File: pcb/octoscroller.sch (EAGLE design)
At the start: 5 parts

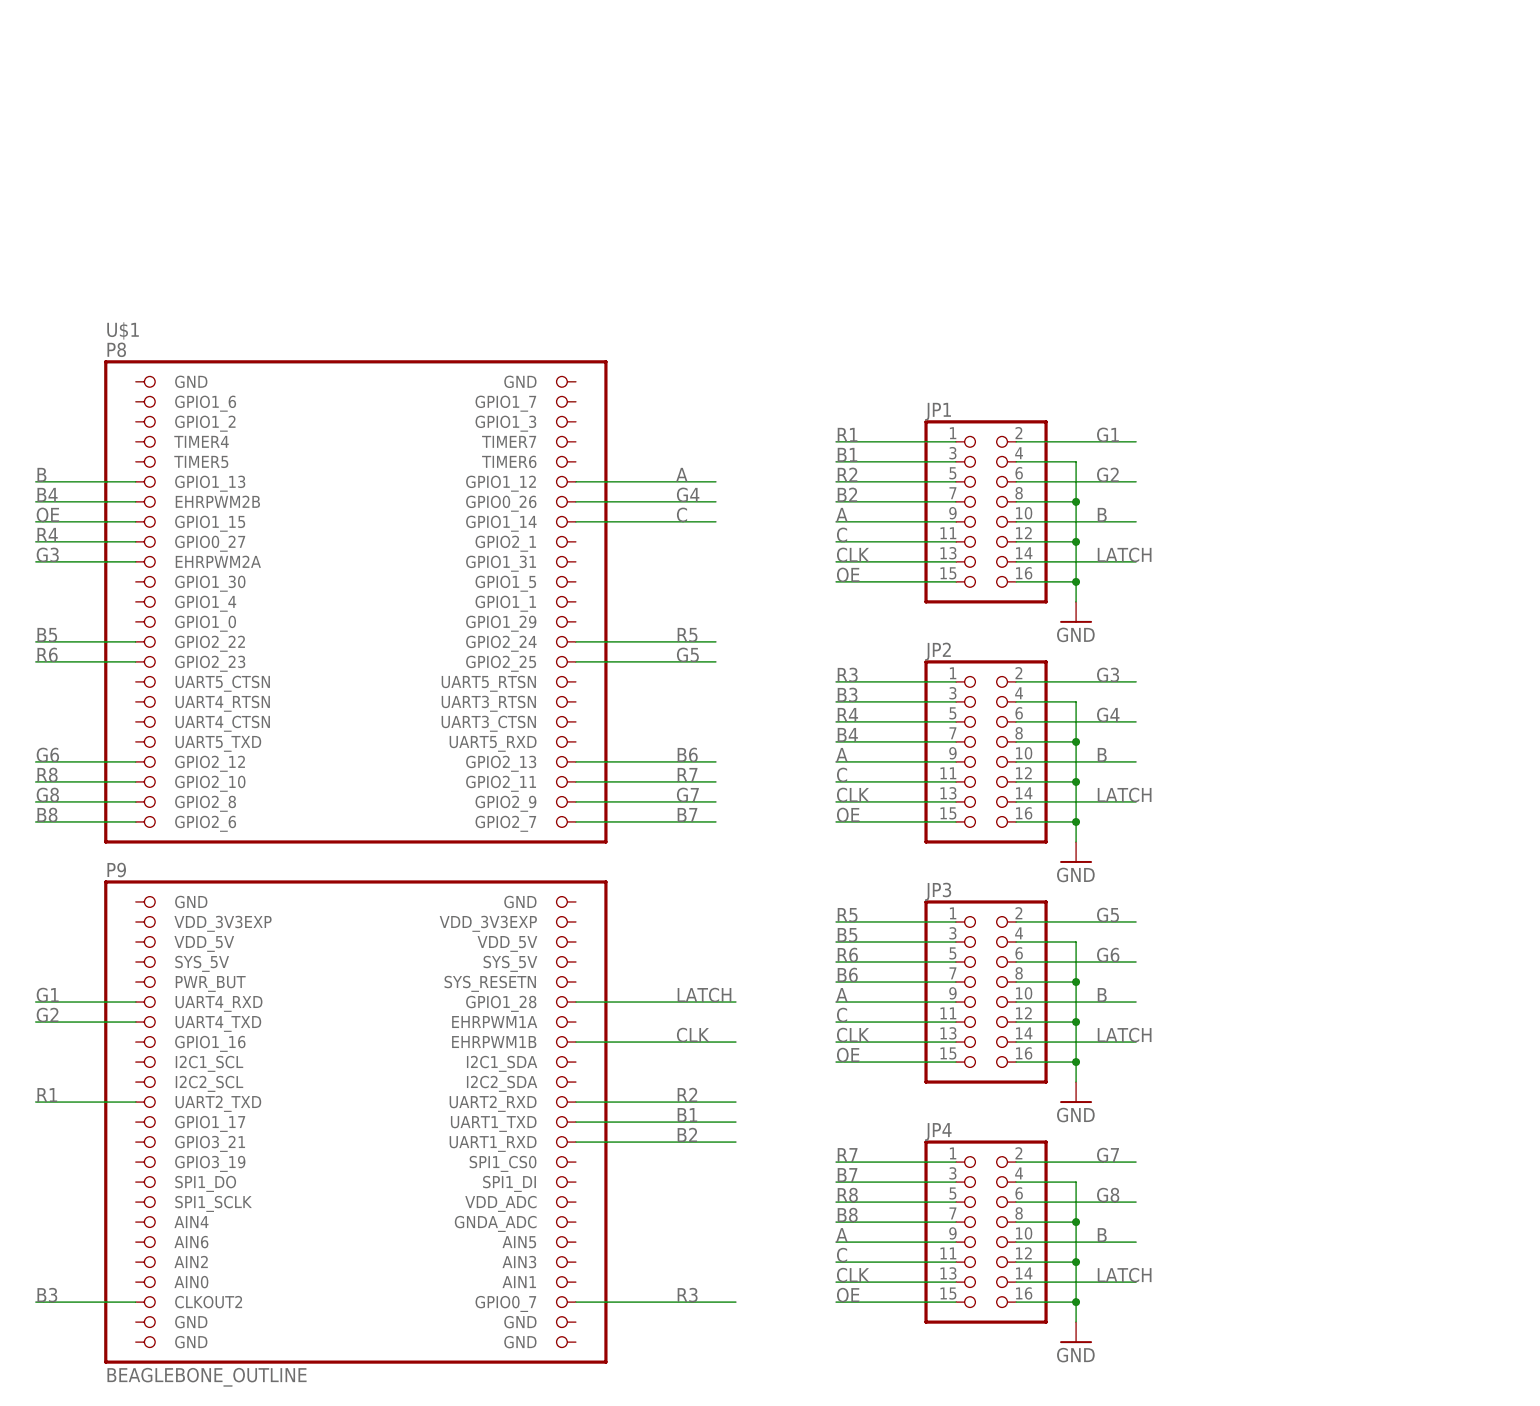
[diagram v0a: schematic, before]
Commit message: octoscroller gets octo-outputs
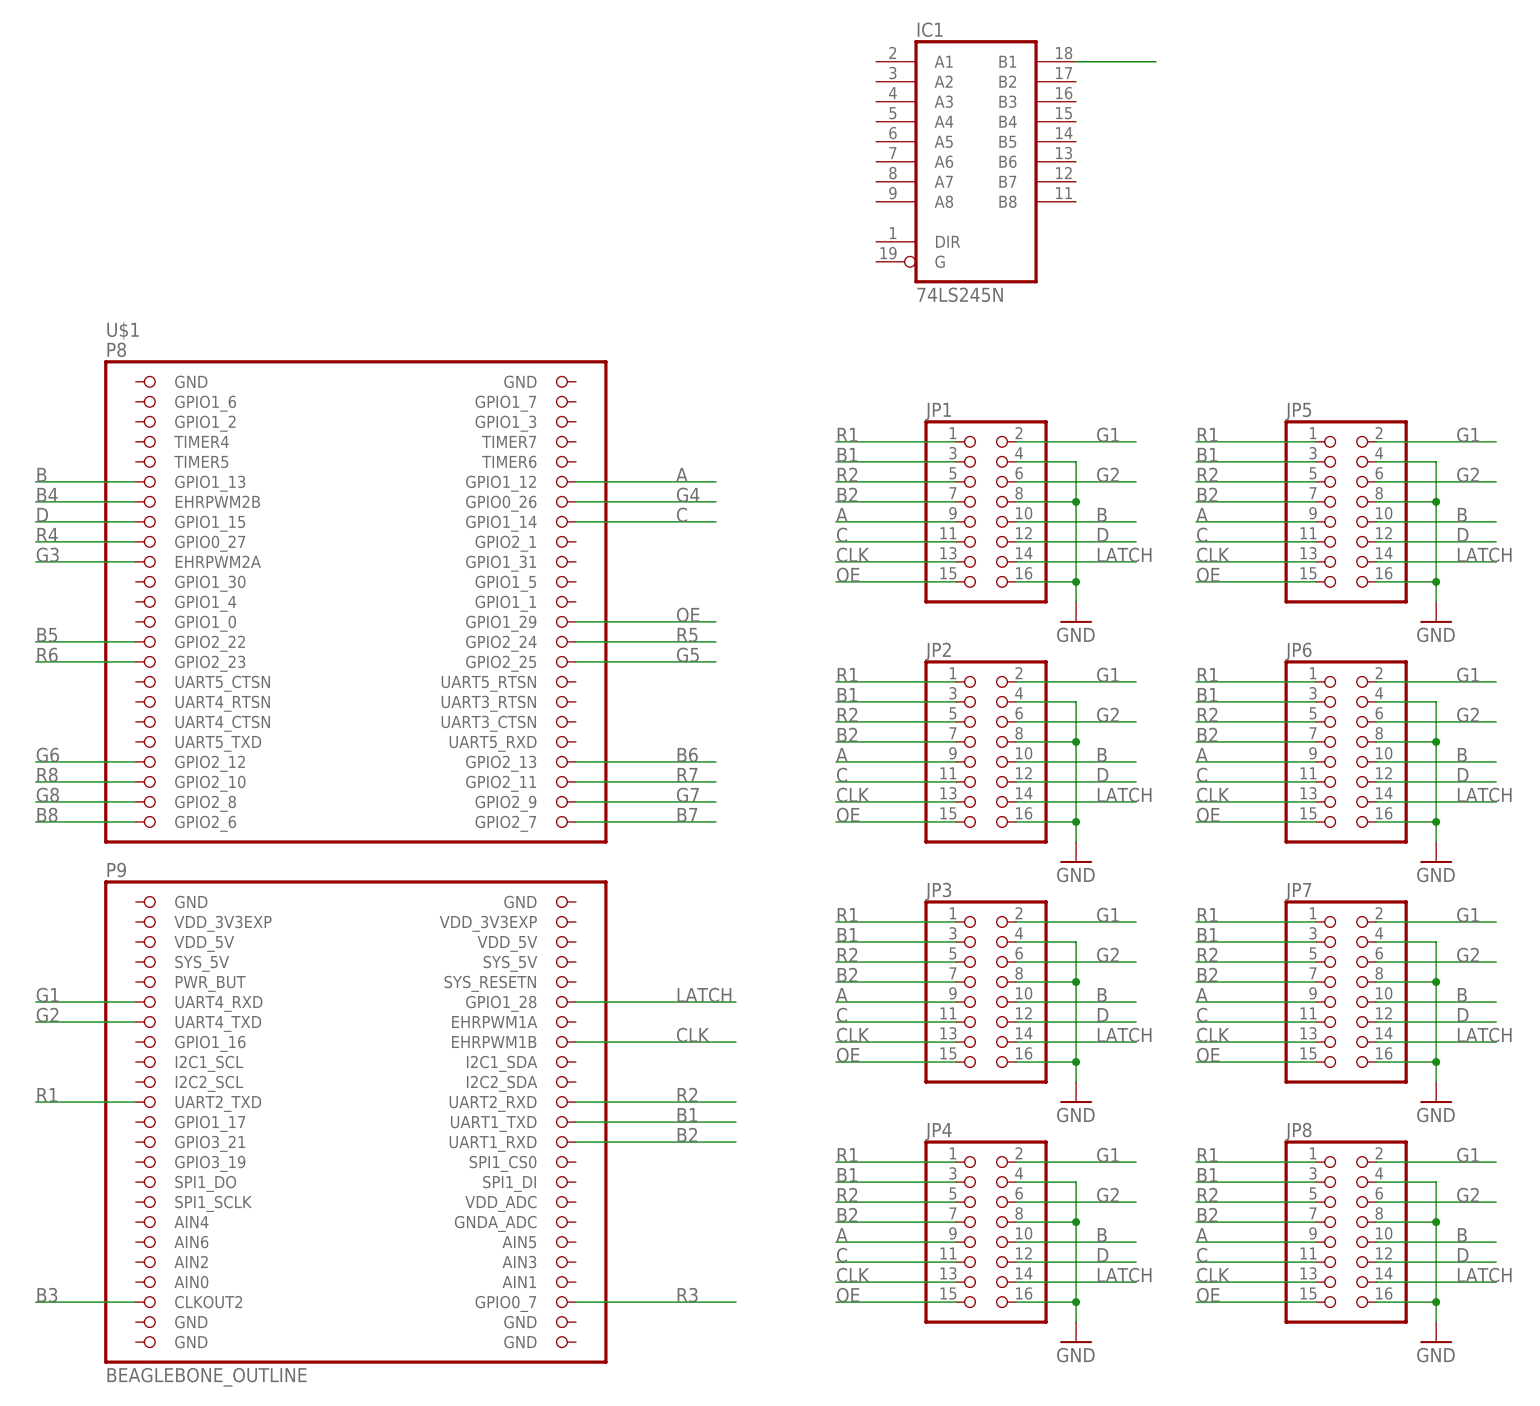
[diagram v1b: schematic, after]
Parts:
- added IC1: 74LS245N, adafruit:74LS245N
- added JP5, JP6, JP7, JP8: (no value), pinhead:PINHD-2X8
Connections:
- new net D: JP1.12, JP2.12, JP3.12, JP4.12, JP5.12, JP6.12, JP7.12, JP8.12, U$1.GPIO1_15
- new net N$1: IC1A.B1
- net A: now also JP5.9, JP6.9, JP7.9, JP8.9
- net B: now also JP5.10, JP6.10, JP7.10, JP8.10
- net B1: now also JP2.3, JP3.3, JP4.3, JP5.3, JP6.3, JP7.3, JP8.3
- net B2: now also JP2.7, JP3.7, JP4.7, JP5.7, JP6.7, JP7.7, JP8.7
- net B3: no longer JP2.3
- net B4: no longer JP2.7
- net B5: no longer JP3.3
- net B6: no longer JP3.7
- net B7: no longer JP4.3
- net B8: no longer JP4.7
- net C: now also JP5.11, JP6.11, JP7.11, JP8.11
- net CLK: now also JP5.13, JP6.13, JP7.13, JP8.13
- net G1: now also JP2.2, JP3.2, JP4.2, JP5.2, JP6.2, JP7.2, JP8.2
- net G2: now also JP2.6, JP3.6, JP4.6, JP5.6, JP6.6, JP7.6, JP8.6
- net G3: no longer JP2.2
- net G4: no longer JP2.6
- net G5: no longer JP3.2
- net G6: no longer JP3.6
- net G7: no longer JP4.2
- net G8: no longer JP4.6
- net GND: now also JP5.16, JP5.4, JP5.8, JP6.16, JP6.4, JP6.8, JP7.16, JP7.4, JP7.8, JP8.16, JP8.4, JP8.8; no longer JP1.12, JP2.12, JP3.12, JP4.12
- net LATCH: now also JP5.14, JP6.14, JP7.14, JP8.14
- net OE: now also JP5.15, JP6.15, JP7.15, JP8.15, U$1.GPIO1_29; no longer U$1.GPIO1_15
- net R1: now also JP2.1, JP3.1, JP4.1, JP5.1, JP6.1, JP7.1, JP8.1
- net R2: now also JP2.5, JP3.5, JP4.5, JP5.5, JP6.5, JP7.5, JP8.5
- net R3: no longer JP2.1
- net R4: no longer JP2.5
- net R5: no longer JP3.1
- net R6: no longer JP3.5
- net R7: no longer JP4.1
- net R8: no longer JP4.5

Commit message: octoscroller renamed outputs
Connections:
- removed net B4: U$1.EHRPWM2B
- removed net B5: U$1.GPIO2_22
- removed net G3: U$1.EHRPWM2A
- removed net G4: U$1.GPIO0_26
- removed net G5: U$1.GPIO2_25
- removed net N$1: IC1A.B1
- removed net R4: U$1.GPIO0_27
- removed net R5: U$1.GPIO2_24
- removed net R6: U$1.GPIO2_23
- new net A_RAW: IC1A.B1, U$1.GPIO1_12
- new net B1.1: JP1.3, U$1.TIMER5
- new net B1.2: JP1.7, U$1.GPIO0_26
- new net B2.1: JP2.3, U$1.EHRPWM2A
- new net B2.2: JP2.7, U$1.GPIO2_24
- new net B3.1: JP3.3
- new net B3.2: JP3.7
- new net B4.1: JP4.3
- new net B4.2: JP4.7
- new net B5.1: JP5.3
- new net B5.2: JP5.7
- new net B6.1: JP6.3
- new net B6.2: JP6.7
- new net B7.1: JP7.3
- new net B7.2: JP7.7
- new net B8.1: JP8.3
- new net B8.2: JP8.7
- new net B_RAW: IC1A.B2, U$1.GPIO1_13
- new net CLK_RAW: IC1A.B6, U$1.EHRPWM1B
- new net C_RAW: IC1A.B3, U$1.GPIO1_14
- new net D_RAW: IC1A.B4, U$1.GPIO1_15
- new net G1.1: JP1.2, U$1.TIMER7
- new net G1.2: JP1.6, U$1.TIMER6
- new net G2.1: JP2.2, U$1.GPIO2_1
- new net G2.2: JP2.6, U$1.GPIO2_23
- new net G3.1: JP3.2
- new net G3.2: JP3.6
- new net G4.1: JP4.2
- new net G4.2: JP4.6
- new net G5.1: JP5.2
- new net G5.2: JP5.6
- new net G6.1: JP6.2
- new net G6.2: JP6.6
- new net G7.1: JP7.2
- new net G7.2: JP7.6
- new net G8.1: JP8.2
- new net G8.2: JP8.6
- new net LATCH_RAW: IC1A.B7, U$1.GPIO1_28
- new net N$11: U$1.UART5_RTSN
- new net N$12: U$1.UART3_RTSN
- new net N$13: U$1.UART3_CTSN
- new net N$14: U$1.UART5_RXD
- new net N$15: U$1.GPIO1_16
- new net N$16: U$1.I2C1_SCL
- new net N$17: U$1.GPIO1_17
- new net N$18: U$1.GPIO3_21
- new net N$19: U$1.GPIO3_19
- new net N$20: U$1.SPI1_DO
- new net N$21: U$1.SPI1_SCLK
- new net N$22: U$1.EHRPWM1A
- new net N$23: U$1.SPI1_CS0
- new net N$24: U$1.SPI1_DI
- new net N$4: U$1.UART5_CTSN
- new net N$5: U$1.UART4_RTSN
- new net N$6: U$1.UART4_CTSN
- new net N$7: U$1.UART5_TXD
- new net OE_RAW: IC1A.B5, U$1.GPIO1_29
- new net R1.1: JP1.1, U$1.TIMER4
- new net R1.2: JP1.5, U$1.EHRPWM2B
- new net R2.1: JP2.1, U$1.GPIO0_27
- new net R2.2: JP2.5, U$1.GPIO2_22
- new net R3.1: JP3.1
- new net R3.2: JP3.5
- new net R4.1: JP4.1
- new net R4.2: JP4.5
- new net R5.1: JP5.1, U$1.GPIO2_25
- new net R5.2: JP5.5
- new net R6.1: JP6.1
- new net R6.2: JP6.5
- new net R7.1: JP7.1
- new net R7.2: JP7.5
- new net R8.1: JP8.1
- new net R8.2: JP8.5
- net A: now also IC1A.A1; no longer U$1.GPIO1_12
- net B: now also IC1A.A2; no longer U$1.GPIO1_13
- net B1: no longer JP1.3, JP2.3, JP3.3, JP4.3, JP5.3, JP6.3, JP7.3, JP8.3
- net B2: no longer JP1.7, JP2.7, JP3.7, JP4.7, JP5.7, JP6.7, JP7.7, JP8.7
- net C: now also IC1A.A3; no longer U$1.GPIO1_14
- net CLK: now also IC1A.A6; no longer U$1.EHRPWM1B
- net D: now also IC1A.A4; no longer U$1.GPIO1_15
- net G1: no longer JP1.2, JP2.2, JP3.2, JP4.2, JP5.2, JP6.2, JP7.2, JP8.2
- net G2: no longer JP1.6, JP2.6, JP3.6, JP4.6, JP5.6, JP6.6, JP7.6, JP8.6
- net GND: now also IC1A.DIR, IC1A.G
- net LATCH: now also IC1A.A7; no longer U$1.GPIO1_28
- net OE: now also IC1A.A5; no longer U$1.GPIO1_29
- net R1: no longer JP1.1, JP2.1, JP3.1, JP4.1, JP5.1, JP6.1, JP7.1, JP8.1
- net R2: no longer JP1.5, JP2.5, JP3.5, JP4.5, JP5.5, JP6.5, JP7.5, JP8.5

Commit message: As ordered from OSH Park
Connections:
- removed net B1: U$1.UART1_TXD
- removed net B2: U$1.UART1_RXD
- removed net B3: U$1.CLKOUT2
- removed net B6: U$1.GPIO2_13
- removed net B7: U$1.GPIO2_7
- removed net B8: U$1.GPIO2_6
- removed net G1: U$1.UART4_RXD
- removed net G2: U$1.UART4_TXD
- removed net G6: U$1.GPIO2_12
- removed net G7: U$1.GPIO2_9
- removed net G8: U$1.GPIO2_8
- removed net N$11: U$1.UART5_RTSN
- removed net N$12: U$1.UART3_RTSN
- removed net N$13: U$1.UART3_CTSN
- removed net N$14: U$1.UART5_RXD
- removed net N$15: U$1.GPIO1_16
- removed net N$16: U$1.I2C1_SCL
- removed net N$17: U$1.GPIO1_17
- removed net N$18: U$1.GPIO3_21
- removed net N$19: U$1.GPIO3_19
- removed net N$20: U$1.SPI1_DO
- removed net N$21: U$1.SPI1_SCLK
- removed net N$22: U$1.EHRPWM1A
- removed net N$23: U$1.SPI1_CS0
- removed net N$24: U$1.SPI1_DI
- removed net N$4: U$1.UART5_CTSN
- removed net N$5: U$1.UART4_RTSN
- removed net N$6: U$1.UART4_CTSN
- removed net N$7: U$1.UART5_TXD
- removed net R1: U$1.UART2_TXD
- removed net R2: U$1.UART2_RXD
- removed net R3: U$1.GPIO0_7
- removed net R7: U$1.GPIO2_11
- removed net R8: U$1.GPIO2_10
- new net +5V: IC1P.VCC, U$1.SYS_5V@1
- net B3.1: now also U$1.UART4_TXD
- net B3.2: now also U$1.I2C1_SCL
- net B4.1: now also U$1.GPIO1_17
- net B4.2: now also U$1.I2C1_SDA
- net B5.1: now also U$1.UART5_CTSN
- net B5.2: now also U$1.UART3_RTSN
- net B6.1: now also U$1.UART5_TXD
- net B6.2: now also U$1.GPIO2_12
- net B7.1: now also U$1.GPIO2_8
- net B7.2: now also U$1.GPIO2_7
- net B8.1: now also U$1.SPI1_DO
- net B8.2: now also U$1.CLKOUT2
- net G3.1: now also U$1.EHRPWM1A
- net G3.2: now also U$1.UART2_TXD
- net G4.1: now also U$1.UART1_TXD
- net G4.2: now also U$1.GPIO3_19
- net G5.1: now also U$1.UART5_RTSN
- net G5.2: now also U$1.UART4_CTSN
- net G6.1: now also U$1.UART5_RXD
- net G6.2: now also U$1.GPIO2_10
- net G7.1: now also U$1.GPIO2_9
- net G7.2: now also U$1.GPIO0_7
- net G8.1: now also U$1.SPI1_DI
- net G8.2: now also U$1.UART1_RXD
- net GND: now also IC1P.GND, U$1.GND@1
- net R3.1: now also U$1.UART4_RXD
- net R3.2: now also U$1.GPIO1_16
- net R4.1: now also U$1.UART2_RXD
- net R4.2: now also U$1.GPIO3_21
- net R5.2: now also U$1.UART4_RTSN
- net R6.1: now also U$1.UART3_CTSN
- net R6.2: now also U$1.GPIO2_13
- net R7.1: now also U$1.GPIO2_11
- net R7.2: now also U$1.GPIO2_6
- net R8.1: now also U$1.SPI1_CS0
- net R8.2: now also U$1.SPI1_SCLK
